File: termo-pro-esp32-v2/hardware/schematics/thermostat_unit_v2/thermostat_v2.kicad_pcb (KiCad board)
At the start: 2 copper layers, 169 x 87 mm, 26 parts, among them J1 Conn_01x08_Pin, Q1 PN2222A, Q2 PN2222A, SW1 SW_Push, SW2 SW_Push, SW3 SW_Push, SW4 SW_Push, U1 NODEMCU-32S, U2 DHT11

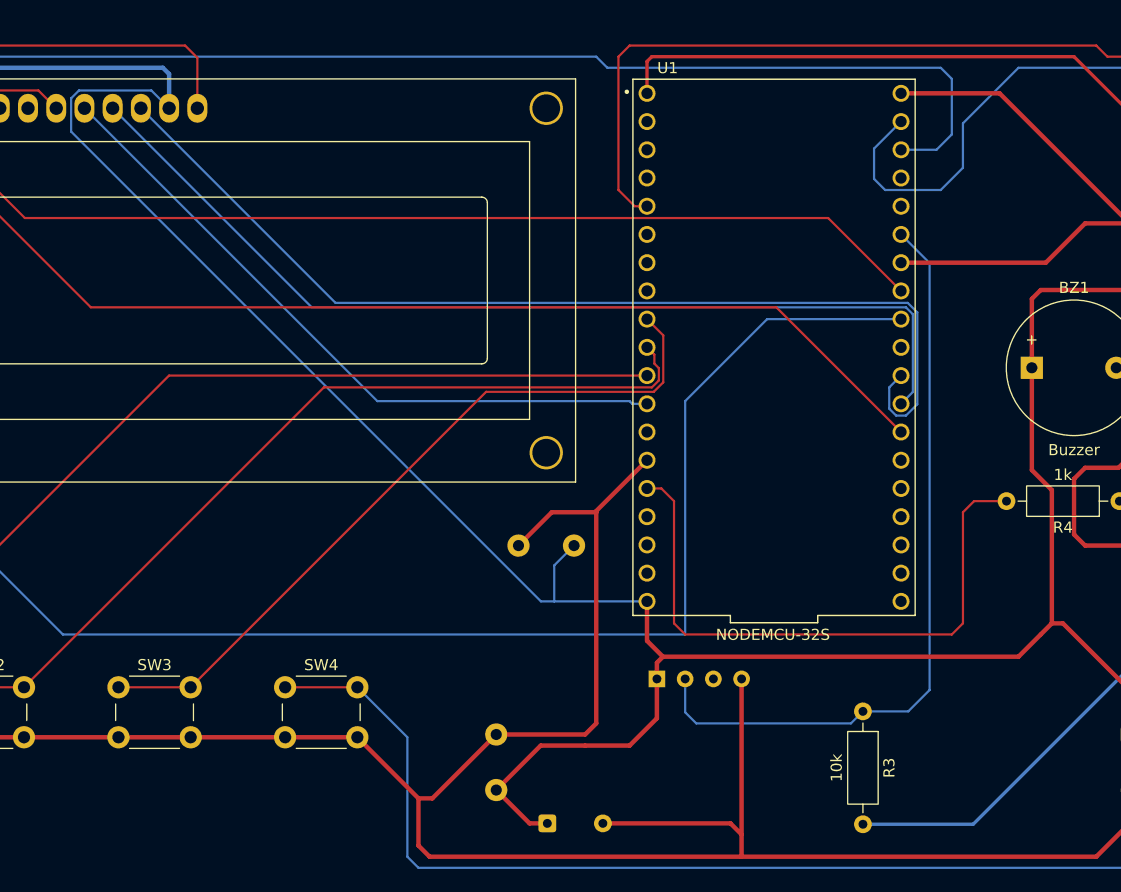
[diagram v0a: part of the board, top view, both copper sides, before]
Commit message: minor thermostat pcb and schematic fix , missed to put the 3.3V net to DHT11, put the 5V instead, mistake
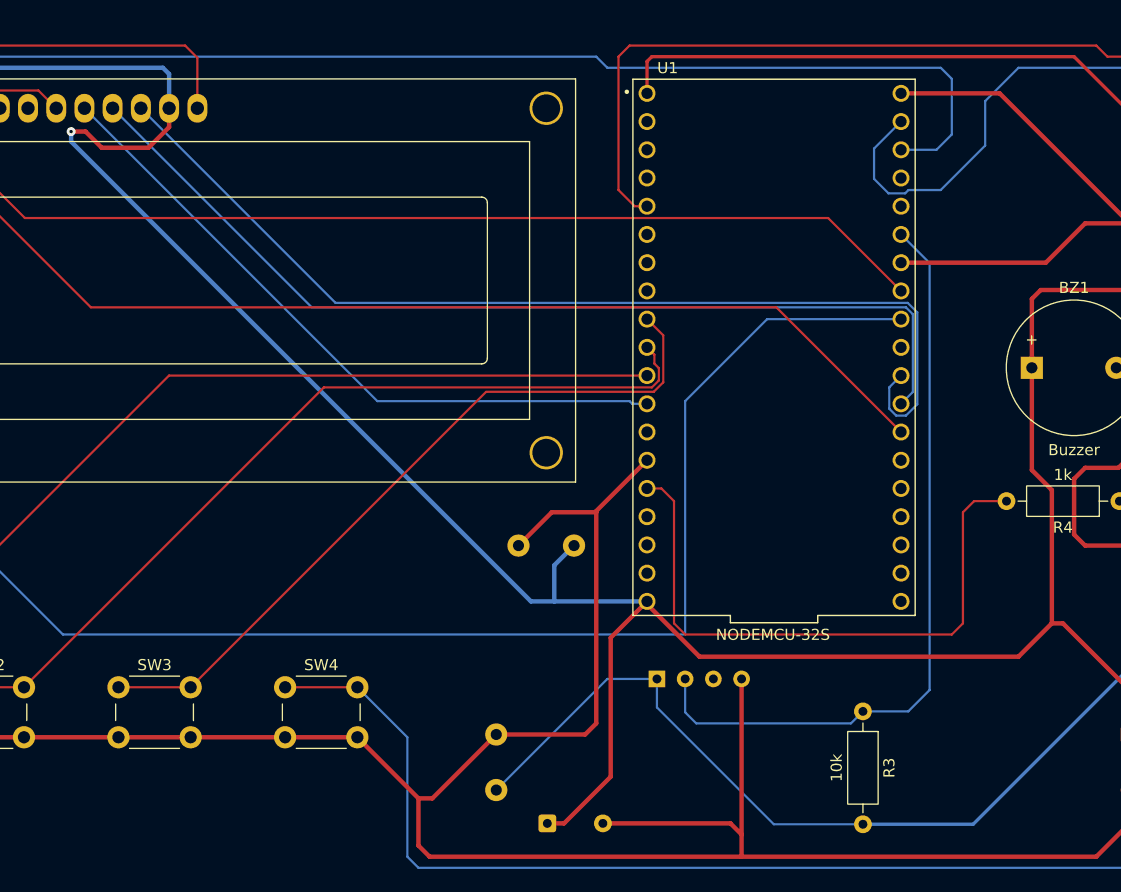
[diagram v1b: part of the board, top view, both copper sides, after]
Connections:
- C4 pad 2: /+VDC -> /V(3.3)
- U2 pad 1: /+VDC -> /V(3.3)
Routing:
- net /V(3.3): track 147.8 -> 191.9 mm
- net /+VDC: track 315.7 -> 309.3 mm, vias 0 -> 1
